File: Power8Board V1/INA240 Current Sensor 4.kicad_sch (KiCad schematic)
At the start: 3 parts, among them U7 INA240A2PWR

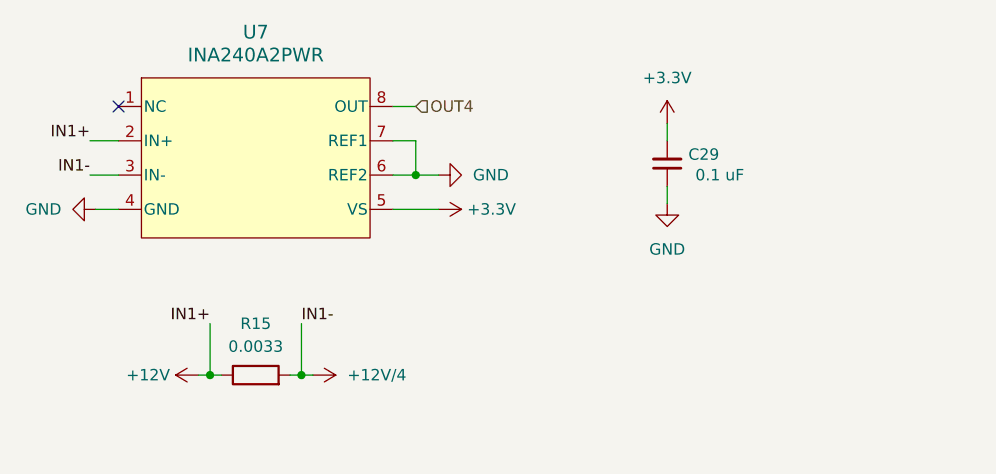
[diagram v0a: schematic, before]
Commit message: Laid out components
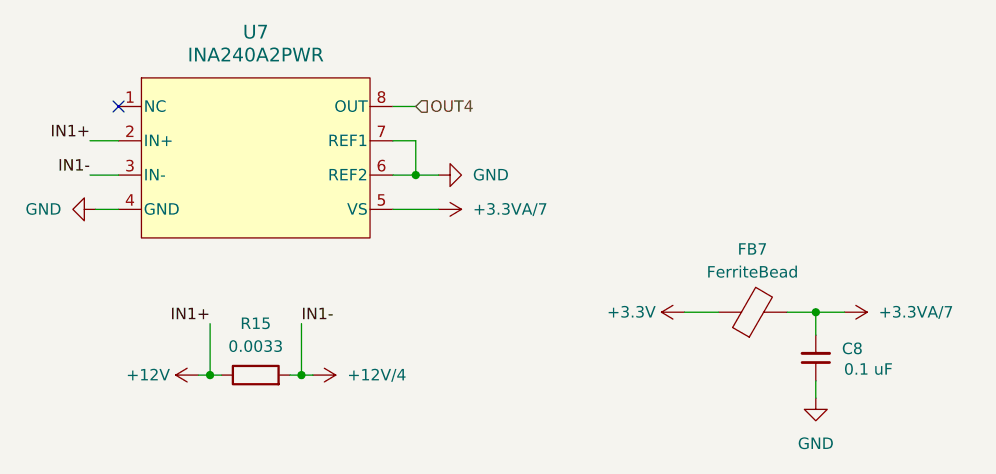
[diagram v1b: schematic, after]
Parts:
- removed C29: 0.1 uF, 0805 Ceramic Capacitor:CAPC2012X140N, symbol Device:C_Small
- added C8: 0.1 uF, 0805 Ceramic Capacitor:CAPC2012X140N, symbol Device:C_Small
- added FB7: FerriteBead, MPZ2012S102ATD25:BEADC2012X105N, symbol Device:FerriteBead
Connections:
- net +3.3V: now also FB7.1; no longer U7.5 (VS)
- net GND: now also C8.1
- new net +3.3VA/7: C8.2, FB7.2, U7.5 (VS)
